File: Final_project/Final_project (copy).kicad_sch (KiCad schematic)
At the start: 30 parts, among them J1 USB4105-GF-A, U1 RP2040, U2 MCP1702T-3302E_CB, U3 W25Q128JV, Y1 12MHz

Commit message: Add pinouts for connectors
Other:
- note added: "SDA SCL"
- note added: "connector"
- note added: "match LCD order!"
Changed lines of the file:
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@@
+    (stroke (width 0) (type default) (color 0 0 0 0))
+  )
+  (polyline (pts (xy 240.03 111.76) (xy 248.92 111.76))
     (stroke (width 0) (type default) (color 0 0 0 0))
   )
@@
     (stroke (width 0) (type default) (color 0 0 0 0))
   )
+  (polyline (pts (xy 240.03 100.33) (xy 248.92 100.33))
+    (stroke (width 0) (type default) (color 0 0 0 0))
+  )
   (wire (pts (xy 46.99 49.53) (xy 46.99 50.8))
     (stroke (width 0) (type default) (color 0 0 0 0))
@@
     (stroke (width 0) (type default) (color 0 0 0 0))
   )
+  (polyline (pts (xy 248.92 111.76) (xy 248.92 100.33))
+    (stroke (width 0) (type default) (color 0 0 0 0))
+  )
   (wire (pts (xy 72.39 173.99) (xy 76.2 173.99))
     (stroke (width 0) (type default) (color 0 0 0 0))
@@
     (stroke (width 0) (type default) (color 0 0 0 0))
   )
+  (wire (pts (xy 147.32 57.15) (xy 156.21 57.15))
+    (stroke (width 0) (type default) (color 0 0 0 0))
+  )
   (wire (pts (xy 72.39 143.51) (xy 72.39 158.75))
     (stroke (width 0) (type default) (color 0 0 0 0))
@@
     (stroke (width 0) (type default) (color 0 0 0 0))
   )
+  (wire (pts (xy 147.32 52.07) (xy 156.21 52.07))
+    (stroke (width 0) (type default) (color 0 0 0 0))
+  )
   (wire (pts (xy 72.39 168.91) (xy 76.2 168.91))
     (stroke (width 0) (type default) (color 0 0 0 0))
@@
     (stroke (width 0) (type default) (color 0 0 0 0))
   )
+  (polyline (pts (xy 240.03 100.33) (xy 240.03 111.76))
+    (stroke (width 0) (type default) (color 0 0 0 0))
+  )
   (wire (pts (xy 85.09 128.27) (xy 86.36 128.27))
     (stroke (width 0) (type default) (color 0 0 0 0))
@@
   (wire (pts (xy 73.66 41.91) (xy 76.2 41.91))
     (stroke (width 0) (type default) (color 0 0 0 0))
+  )
+  (text "match LCD order!" (at 257.81 96.52 0)
+    (effects (font (size 1.27 1.27)) (justify left bottom))
   )
   (text "Power Flags" (at 265.43 143.51 0)
     (effects (font (size 1.27 1.27) (thickness 0.254) bold) (justify left bottom))
   )
+  (text "SDA\n\nSCL" (at 269.24 110.49 0)
+    (effects (font (size 1.27 1.27)) (justify left bottom))
+  )
   (text "RP2040 Datasheet\n\n10 SPI1 SCK\n11 SPI1 TX -> MOSI\n12 SPI1 RX -> MISO\n13 SPI1 CSn"
     (at 214.63 82.55 0)
     (effects (font (size 1.27 1.27)) (justify left bottom))
   )
+  (text "connector" (at 241.3 99.06 0)
+    (effects (font (size 1.27 1.27)) (justify left bottom))
+  )
   (label "GPIO14" (at 147.32 113.03 0)
     (effects (font (size 1.27 1.27)) (justify left bottom))
@@
     (effects (font (size 1.27 1.27)) (justify left bottom))
   )
+  (label "SDA" (at 254 105.41 0)
+    (effects (font (size 1.27 1.27)) (justify left bottom))
+  )
   (label "SWCLK" (at 86.36 77.47 180)
     (effects (font (size 1.27 1.27)) (justify right bottom))
@@
     (effects (font (size 1.27 1.27)) (justify left bottom))
   )
-  (label "GPIO14" (at 207.01 109.22 0)
-    (effects (font (size 1.27 1.27)) (justify left bottom))
-  )
   (label "GPIO28" (at 147.32 184.15 0)
     (effects (font (size 1.27 1.27)) (justify left bottom))
@@
     (effects (font (size 1.27 1.27)) (justify left bottom))
   )
+  (label "SDA" (at 156.21 52.07 0)
+    (effects (font (size 1.27 1.27)) (justify left bottom))
+  )
   (label "GPIO7" (at 147.32 77.47 0)
     (effects (font (size 1.27 1.27)) (justify left bottom))
@@
     (effects (font (size 1.27 1.27)) (justify left bottom))
   )
+  (label "SCL" (at 254 110.49 0)
+    (effects (font (size 1.27 1.27)) (justify left bottom))
+  )
   (label "GPIO18" (at 147.32 133.35 0)
     (effects (font (size 1.27 1.27)) (justify left bottom))
   )
   (label "GPIO29" (at 147.32 189.23 0)
+    (effects (font (size 1.27 1.27)) (justify left bottom))
+  )
+  (label "VBUS" (at 254 101.6 0)
     (effects (font (size 1.27 1.27)) (justify left bottom))
   )
@@
     (effects (font (size 1.27 1.27)) (justify right bottom))
   )
+  (label "SCL" (at 156.21 57.15 0)
+    (effects (font (size 1.27 1.27)) (justify left bottom))
+  )
   (label "GPIO1" (at 147.32 46.99 0)
     (effects (font (size 1.27 1.27)) (justify left bottom))
   )
+  (label "GPIO0" (at 207.01 109.22 0)
+    (effects (font (size 1.27 1.27)) (justify left bottom))
+  )
   (symbol (lib_id "Device:C") (at 80.01 138.43 270) (unit 1)
     (in_bom yes) (on_board yes)
@@
     (pin "1")
     (pin "2")
+  )
+  (symbol (lib_id "power:GND") (at 254 113.03 0) (unit 1)
+    (in_bom yes) (on_board yes)
+    (property "Reference" "#PWR?" (id 0) (at 254 119.38 0)
+      (effects (font (size 1.27 1.27)) hide)
+    )
+    (property "Value" "GND" (id 1) (at 254 118.11 0))
+    (property "Footprint" "" (id 2) (at 254 113.03 0)
+      (effects (font (size 1.27 1.27)) hide)
+    )
+    (property "Datasheet" "" (id 3) (at 254 113.03 0)
+      (effects (font (size 1.27 1.27)) hide)
+    )
+    (pin "1")
   )
   (symbol (lib_id "Device:C") (at 80.01 179.07 270) (unit 1)
@@
       (reference "#PWR0138") (unit 1) (value "GND") (footprint "")
     )
+    (path "/07e08d6f-13bf-438c-b011-d02667cb70f7"
+      (reference "#PWR?") (unit 1) (value "GND") (footprint "")
+    )
     (path "/4185e825-d3db-49f7-84c3-1d674f768766"

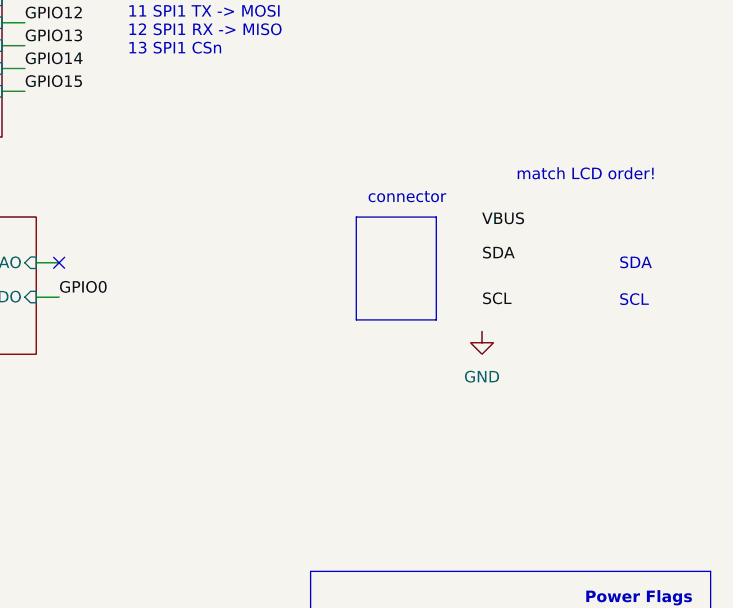
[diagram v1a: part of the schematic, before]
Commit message: Add horizontal pin connect
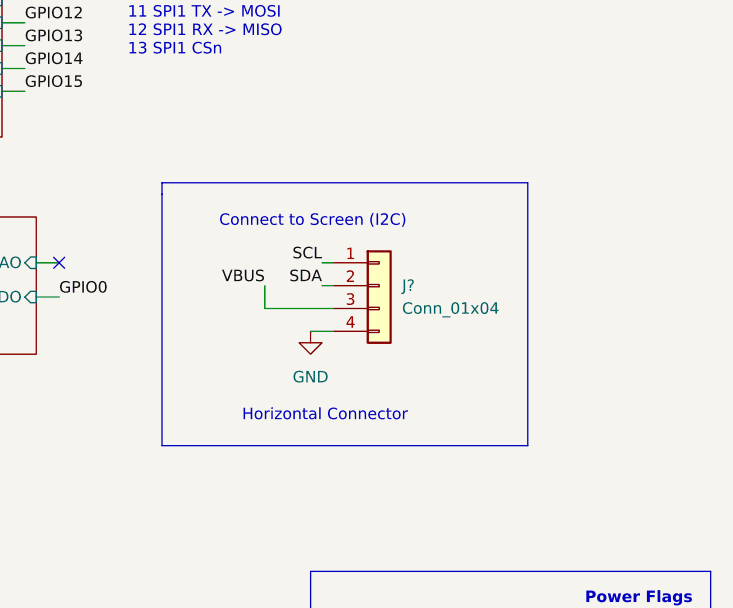
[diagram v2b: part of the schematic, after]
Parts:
- added J?: Conn_01x04, Connector_PinSocket_2.54mm:PinSocket_1x04_P2.54mm_Horizontal, symbol Connector_Generic:Conn_01x04
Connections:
- net GND: now also J?.4 (Pin_4)
- net GPIO2: now also J?.2 (Pin_2)
- net GPIO3: now also J?.1 (Pin_1)
- net VBUS: now also J?.3 (Pin_3)
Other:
- note added: "Connect to Screen (I2C)"
- note added: "Horizontal Connector"
- note removed: "SDA SCL"
- note removed: "connector"
- note removed: "match LCD order!"
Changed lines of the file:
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@@
-    (stroke (width 0) (type default) (color 0 0 0 0))
-  )
-  (polyline (pts (xy 240.03 111.76) (xy 248.92 111.76))
     (stroke (width 0) (type default) (color 0 0 0 0))
   )
@@
     (stroke (width 0) (type default) (color 0 0 0 0))
   )
+  (wire (pts (xy 237.49 110.49) (xy 229.87 110.49))
+    (stroke (width 0) (type default) (color 0 0 0 0))
+  )
   (wire (pts (xy 29.21 118.11) (xy 29.21 119.38))
     (stroke (width 0) (type default) (color 0 0 0 0))
@@
     (stroke (width 0) (type default) (color 0 0 0 0))
   )
-  (polyline (pts (xy 240.03 100.33) (xy 248.92 100.33))
-    (stroke (width 0) (type default) (color 0 0 0 0))
-  )
   (wire (pts (xy 46.99 49.53) (xy 46.99 50.8))
     (stroke (width 0) (type default) (color 0 0 0 0))
@@
     (stroke (width 0) (type default) (color 0 0 0 0))
   )
+  (wire (pts (xy 229.87 110.49) (xy 229.87 107.95))
+    (stroke (width 0) (type default) (color 0 0 0 0))
+  )
   (wire (pts (xy 86.36 123.19) (xy 85.09 123.19))
     (stroke (width 0) (type default) (color 0 0 0 0))
@@
     (stroke (width 0) (type default) (color 0 0 0 0))
   )
+  (polyline (pts (xy 259.08 125.73) (xy 259.08 96.52))
+    (stroke (width 0) (type default) (color 0 0 0 0))
+  )
   (wire (pts (xy 30.48 118.11) (xy 29.21 118.11))
     (stroke (width 0) (type default) (color 0 0 0 0))
@@
     (stroke (width 0) (type default) (color 0 0 0 0))
   )
-  (polyline (pts (xy 248.92 111.76) (xy 248.92 100.33))
+  (wire (pts (xy 236.22 105.41) (xy 237.49 105.41))
     (stroke (width 0) (type default) (color 0 0 0 0))
   )
@@
     (stroke (width 0) (type default) (color 0 0 0 0))
   )
+  (polyline (pts (xy 218.44 125.73) (xy 259.08 125.73))
+    (stroke (width 0) (type default) (color 0 0 0 0))
+  )
+  (wire (pts (xy 236.22 107.95) (xy 237.49 107.95))
+    (stroke (width 0) (type default) (color 0 0 0 0))
+  )
+  (polyline (pts (xy 218.44 97.79) (xy 218.44 125.73))
+    (stroke (width 0) (type default) (color 0 0 0 0))
+  )
   (wire (pts (xy 72.39 173.99) (xy 72.39 168.91))
     (stroke (width 0) (type default) (color 0 0 0 0))
@@
     (stroke (width 0) (type default) (color 0 0 0 0))
   )
+  (wire (pts (xy 234.95 113.03) (xy 237.49 113.03))
+    (stroke (width 0) (type default) (color 0 0 0 0))
+  )
   (wire (pts (xy 66.04 97.79) (xy 86.36 97.79))
     (stroke (width 0) (type default) (color 0 0 0 0))
@@
     (stroke (width 0) (type default) (color 0 0 0 0))
   )
+  (polyline (pts (xy 218.44 96.52) (xy 218.44 97.79))
+    (stroke (width 0) (type default) (color 0 0 0 0))
+  )
   (wire (pts (xy 66.04 92.71) (xy 67.31 92.71))
     (stroke (width 0) (type default) (color 0 0 0 0))
   )
-  (polyline (pts (xy 240.03 100.33) (xy 240.03 111.76))
-    (stroke (width 0) (type default) (color 0 0 0 0))
-  )
   (wire (pts (xy 85.09 128.27) (xy 86.36 128.27))
     (stroke (width 0) (type default) (color 0 0 0 0))
@@
     (stroke (width 0) (type default) (color 0 0 0 0))
   )
+  (polyline (pts (xy 218.44 96.52) (xy 259.08 96.52))
+    (stroke (width 0) (type default) (color 0 0 0 0))
+  )
   (wire (pts (xy 46.99 34.29) (xy 68.58 34.29))
     (stroke (width 0) (type default) (color 0 0 0 0))
@@
     (stroke (width 0) (type default) (color 0 0 0 0))
   )
-  (text "match LCD order!" (at 257.81 96.52 0)
+  (text "Connect to Screen (I2C)" (at 224.79 101.6 0)
+    (effects (font (size 1.27 1.27)) (justify left bottom))
+  )
+  (text "Horizontal Connector" (at 227.33 123.19 0)
     (effects (font (size 1.27 1.27)) (justify left bottom))
   )
@@
     (effects (font (size 1.27 1.27) (thickness 0.254) bold) (justify left bottom))
   )
-  (text "SDA\n\nSCL" (at 269.24 110.49 0)
-    (effects (font (size 1.27 1.27)) (justify left bottom))
-  )
   (text "RP2040 Datasheet\n\n10 SPI1 SCK\n11 SPI1 TX -> MOSI\n12 SPI1 RX -> MISO\n13 SPI1 CSn"
     (at 214.63 82.55 0)
     (effects (font (size 1.27 1.27)) (justify left bottom))
   )
-  (text "connector" (at 241.3 99.06 0)
-    (effects (font (size 1.27 1.27)) (justify left bottom))
-  )
   (label "GPIO14" (at 147.32 113.03 0)
     (effects (font (size 1.27 1.27)) (justify left bottom))
@@
     (effects (font (size 1.27 1.27)) (justify left bottom))
   )
-  (label "SDA" (at 254 105.41 0)
-    (effects (font (size 1.27 1.27)) (justify left bottom))
+  (label "SDA" (at 236.22 107.95 180)
+    (effects (font (size 1.27 1.27)) (justify right bottom))
   )
   (label "SWCLK" (at 86.36 77.47 180)
@@
     (effects (font (size 1.27 1.27)) (justify left bottom))
   )
-  (label "SCL" (at 254 110.49 0)
-    (effects (font (size 1.27 1.27)) (justify left bottom))
+  (label "SCL" (at 236.22 105.41 180)
+    (effects (font (size 1.27 1.27)) (justify right bottom))
   )
   (label "GPIO18" (at 147.32 133.35 0)
@@
     (effects (font (size 1.27 1.27)) (justify left bottom))
   )
-  (label "VBUS" (at 254 101.6 0)
-    (effects (font (size 1.27 1.27)) (justify left bottom))
+  (label "VBUS" (at 229.87 107.95 180)
+    (effects (font (size 1.27 1.27)) (justify right bottom))
   )
   (label "GPIO9" (at 147.32 87.63 0)
@@
     (pin "2")
   )
-  (symbol (lib_id "power:GND") (at 254 113.03 0) (unit 1)
-    (in_bom yes) (on_board yes)
-    (property "Reference" "#PWR?" (id 0) (at 254 119.38 0)
-      (effects (font (size 1.27 1.27)) hide)
-    )
-    (property "Value" "GND" (id 1) (at 254 118.11 0))
-    (property "Footprint" "" (id 2) (at 254 113.03 0)
-      (effects (font (size 1.27 1.27)) hide)
-    )
-    (property "Datasheet" "" (id 3) (at 254 113.03 0)
+  (symbol (lib_id "power:GND") (at 234.95 113.03 0) (unit 1)
+    (in_bom yes) (on_board yes)
+    (property "Reference" "#PWR?" (id 0) (at 234.95 119.38 0)
+      (effects (font (size 1.27 1.27)) hide)
+    )
+    (property "Value" "GND" (id 1) (at 234.95 118.11 0))
+    (property "Footprint" "" (id 2) (at 234.95 113.03 0)
+      (effects (font (size 1.27 1.27)) hide)
+    )
+    (property "Datasheet" "" (id 3) (at 234.95 113.03 0)
       (effects (font (size 1.27 1.27)) hide)
     )
@@
     (pin "1")
     (pin "2")
+  )
+  (symbol (lib_id "Connector_Generic:Conn_01x04") (at 242.57 107.95 0) (unit 1)
+    (in_bom yes) (on_board yes) (fields_autoplaced)
+    (property "Reference" "J?" (id 0) (at 245.11 107.9499 0)
+      (effects (font (size 1.27 1.27)) (justify left))
+    )
+    (property "Value" "Conn_01x04" (id 1) (at 245.11 110.4899 0)
+      (effects (font (size 1.27 1.27)) (justify left))
+    )
+    (property "Footprint" "Connector_PinSocket_2.54mm:PinSocket_1x04_P2.54mm_Horizontal" (id 2) (at 242.57 107.95 0)
+      (effects (font (size 1.27 1.27)) hide)
+    )
+    (property "Datasheet" "~" (id 3) (at 242.57 107.95 0)
+      (effects (font (size 1.27 1.27)) hide)
+    )
+    (pin "1")
+    (pin "2")
+    (pin "3")
+    (pin "4")
   )
   (symbol (lib_id "Device:C") (at 80.01 158.75 270) (unit 1)
@@
       (reference "J1") (unit 1) (value "USB4105-GF-A") (footprint "Final_project:USB4105-GF-A")
     )
+    (path "/663933f2-4745-4ec0-b4b5-c26901d6bc0c"
+      (reference "J?") (unit 1) (value "Conn_01x04") (footprint "Connector_PinSocket_2.54mm:PinSocket_1x04_P2.54mm_Horizontal")
+    )
     (path "/6e52ec09-aa2b-4fd4-928b-f8255f408a1b"
